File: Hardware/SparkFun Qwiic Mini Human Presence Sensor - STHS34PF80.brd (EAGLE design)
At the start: 25.4 x 12.7 mm, 41 parts, among them J1 Qwiic, J2 Qwiic, U2 STHS34PF80

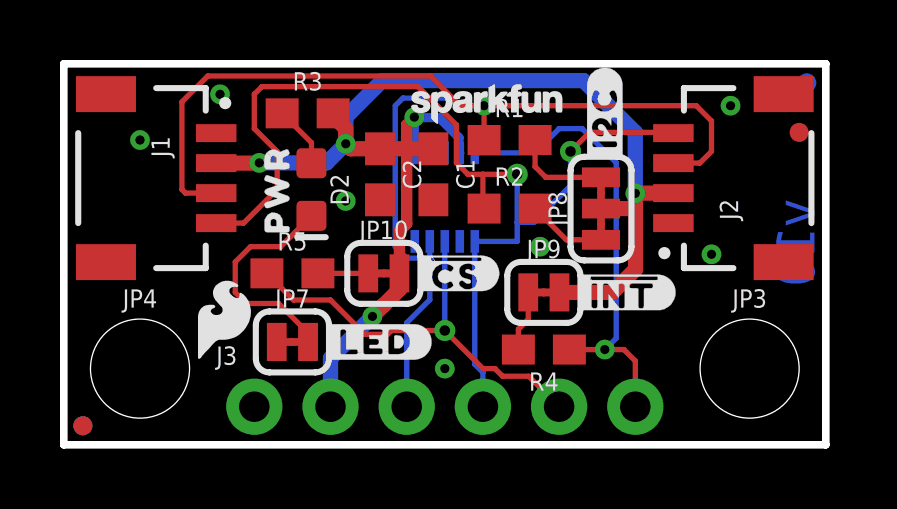
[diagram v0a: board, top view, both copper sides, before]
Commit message: Removed unneeded files; finished design rule errors
Removed the regular Qwiic files and redid the structure of the file folder. Renamed the appropriate files as well. Finished the design rule errors and routing, along with the silk screen. Should be ready for order soon.
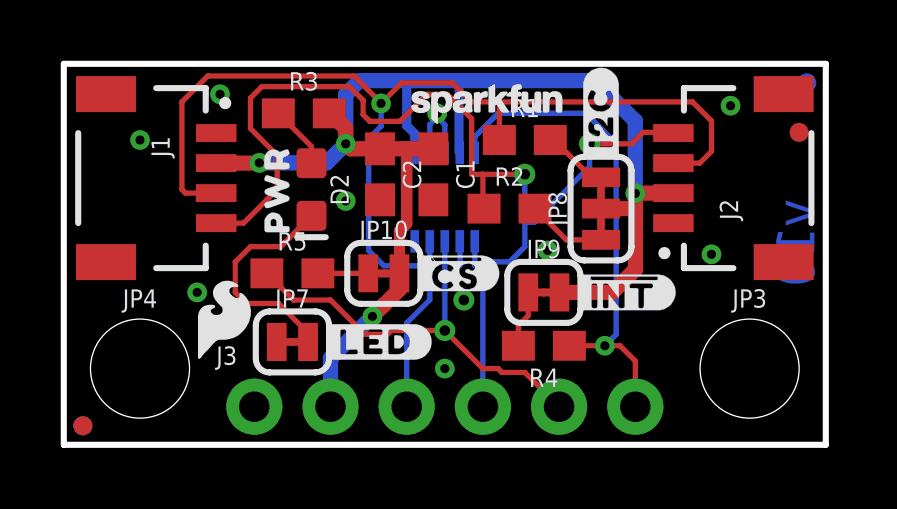
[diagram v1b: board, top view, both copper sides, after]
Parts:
- removed U$6: (no value), output:#INT#8
- added U$13: (no value), output:#GND#35
- U$1: device output:#GND#4 -> output:#3V3#36
- U$2: device output:#3V3#5 -> output:##CS#36
- U$5: device output:##CS#7 -> output:#INT#37
- moved U$2 7.64 mm to (16.5, 3.30)
- moved U$5 2.55 mm to (19.1, 3.56)
- moved U$1 2.54 mm to (8.89, 3.81)
- moved R1 0.51 mm to (15.4, 10.2)
- moved R3 0.13 mm to (8.00, 11.0)
- moved R4 0.13 mm to (16.0, 3.30)
- moved U$8 0.13 mm to (17.9, 10.9)
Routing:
- net GND: track 0.00 -> 3.53 mm, vias 7 -> 10
- net SCL: track 34.4 -> 36.2 mm
- net SDA: track 41.3 -> 40.2 mm
- net 3.3V: track 45.2 -> 46.2 mm, vias 5 -> 4
- net INT: track 15.8 -> 16.8 mm
- net N$2: track 3.23 -> 2.21 mm
